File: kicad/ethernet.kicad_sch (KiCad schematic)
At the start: 6 parts, among them J1 RJ45_Abracon_ARJP11A-MASA-B-A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, U1 TM4C1294NCPDTI3

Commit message: board layout
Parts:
- removed U1: TM4C1294NCPDTI3, QFP40P1600X1600X120-128N, symbol TM4C1294NCPDTI3:TM4C1294NCPDTI3
- added C1, C10, C11, C12, C2, C3, C4, C5, C6, C7, C8, C9: 100n, Capacitor_SMD:C_0805_2012Metric, symbol Device:C_Small
- added C13: 4.7n, Capacitor_SMD:C_0805_2012Metric, symbol Device:C_Small
- added C14: 10n, Capacitor_SMD:C_0805_2012Metric, symbol Device:C_Small
- added J2: Conn_Coaxial, Connector_Coaxial:SMA_Molex_73251-2120_EdgeMount_Horizontal, symbol Connector:Conn_Coaxial
- added L1: 27n, Inductor_SMD:L_0805_2012Metric, symbol Device:L_Small
- added R10: 10, Resistor_SMD:R_0805_2012Metric, symbol Device:R_Small_US
- added R5, R6, R7: 10k, Resistor_SMD:R_0805_2012Metric, symbol Device:R_Small_US
- added R8: 1M, Resistor_SMD:R_0805_2012Metric, symbol Device:R_Small_US
- added R9: 4.87k, Resistor_SMD:R_0805_2012Metric, symbol Device:R_Small_US
- added U1: MSP432E401Y, Package_QFP:LQFP-128_14x14mm_P0.4mm, symbol MCU_Texas:MSP432E401Y
- added U2: MAX-8Q, RF_GPS:ublox_MAX, symbol RF_GPS:MAX-8Q
- added X1: TXEAADSANF-25.000000, Oscillator:Oscillator_SMD_SeikoEpson_SG8002CE-4Pin_3.2x2.5mm, symbol Oscillator:TXC-7C
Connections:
- net +3V3: now also C10.1, C11.1, C12.1, C4.1, C5.1, C6.1, C7.1, C8.1, C9.1, U1.101 (VDD), U1.113 (VDD), U1.122 (VDD), U1.16 (VDD), U1.26 (VDD), U1.28 (VDD), U1.39 (VDD), U1.47 (VDD), U1.51 (VDD), U1.52 (VDD), U1.69 (VDD), U1.7 (VDD), U1.79 (VDD), U1.90 (VDD), U2.6 (V_BCKP), U2.7 (VCC_IO), U2.8 (VCC), X1.4 (Vdd)
- net GND: now also C1.2, C10.2, C11.2, C12.2, C13.2, C14.2, C2.2, C3.2, C4.2, C5.2, C6.2, C7.2, C8.2, C9.2, J2.2 (Ext), R8.1, R9.1, U1.10 (GNDA), U1.114 (GND), U1.17 (GND), U1.48 (GND), U1.55 (GND), U1.58 (GND), U1.80 (GND), U2.1 (GND), U2.10 (GND), U2.12 (GND), X1.2 (GND)
- net at J1.1 (TD+), R4.2: now also U1.57 (EN0TXOP)
- net at J1.15 (SHIELD): now also C13.1, R8.2
- net at J1.2 (TD-), R3.1: now also U1.56 (EN0TXON)
- net at J1.3 (RD+), R2.2: now also U1.54 (EN0RXIP)
- net at J1.6 (RD-), R1.1: now also U1.53 (EN0RXIN)
- new net: J2.1 (In), L1.2, U2.11 (RF_IN)
- new net: R10.1, U2.14 (VCC_RF)
- new net: C14.1, L1.1, R10.2
- new net: C1.1, R5.2, R6.1
- new net: C2.1, R6.2, R7.1
- new net: C3.1, R7.2, X1.1 (EN)
- new net: U1.88 (OSC0), X1.3 (OUT)
- new net: R9.2, U1.59 (RBIAS)
- new net: R5.1, U1.93 (PL7)
- new net gPPS: U1.71 (PM7), U2.4 (TIMEPULSE)
- new net gRX: U1.96 (PB1), U2.3 (RXD)
- new net gTX: U1.95 (PB0), U2.2 (TXD)
- new net uPPS: U1.49 (PG0), U1.72 (PM6)

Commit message: board layout
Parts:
- added C15, C16: 100n, Capacitor_SMD:C_0805_2012Metric, symbol Device:C_Small
- added C17: 2.7u, Capacitor_SMD:C_0805_2012Metric, symbol Device:C_Small
- added J3: MSP-FET, Connector_PinHeader_2.54mm:PinHeader_2x07_P2.54mm_Vertical, symbol Connector_Generic:Conn_02x07_Odd_Even
- added R11, R12: 10k, Resistor_SMD:R_0805_2012Metric, symbol Device:R_Small_US
- added R13, R14: 330, Resistor_SMD:R_0805_2012Metric, symbol Device:R_Small_US
- added SW1, SW2: KSC701, Button_Switch_SMD:SW_Push_1P1T_NO_CK_KSC7xxJ, symbol Switch:SW_Push
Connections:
- net +3V3: now also U1.102 (PQ4), U1.103 (PP2), U1.104 (PP3), U1.105 (PP4), U1.106 (PP5), U1.107 (PN0), U1.108 (PN1), U1.109 (PN2), U1.110 (PN3), U1.111 (PN4), U1.112 (PN5), U1.43 (PF1), U1.44 (PF2), U1.45 (PF3), U1.50 (PG1), U1.60 (PK7), U1.61 (PK6), U1.62 (PK5), U1.63 (PK4), U1.68 (VBAT), U1.75 (PM3), U1.76 (PM2), U1.77 (PM1), U1.78 (PM0), U1.8 (VDDA), U1.81 (PL0), U1.82 (PL1), U1.83 (PL2), U1.84 (PL3), U1.85 (PL4), U1.86 (PL5), U1.9 (VREFA+), U1.91 (PB2), U1.92 (PB3), U1.94 (PL6), J3.4 (Pin_4), R11.2, R12.2
- net GND: now also J1.12 (LLED-), J1.14 (RLED-), C15.2, C16.2, C17.2, J3.9 (Pin_9), SW1.1, SW2.1
- net at J1.11 (LLED+): now also R13.2
- net at J1.13 (RLED+): now also R14.2
- net at U2.5 (EXTINT): now also U1.73 (PM5)
- net at U2.9 (~{RESET}): now also U1.74 (PM4)
- net at U1.100 (PC0/TCK/SWCLK): now also J3.7 (Pin_7)
- net at U1.115 (VDDC): now also U1.87 (VDDC), C15.1, C16.1, C17.1
- net ETH_LED0: now reaches U1.42 (PF0)
- net ETH_LED0: now also R13.1
- net ETH_LED1: now reaches U1.46 (PF4)
- net ETH_LED1: now also R14.1
- net ~{WAKE}: now reaches U1.64 (~{WAKE})
- net ~{WAKE}: now also R12.1, SW2.2
- net ~{RST}: now reaches U1.70 (~{RST})
- net ~{RST}: now also J3.11 (Pin_11), R11.1, SW1.2
- net at U1.97 (PC3/TDO/SWO): now also J3.1 (Pin_1)
- net at U1.98 (PC2/TDI): now also J3.3 (Pin_3)
- net at U1.99 (PC1/TMS/SWDIO): now also J3.5 (Pin_5)
- no-connect marks 0 -> 11

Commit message: board layout
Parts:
- added TR1: Wuerth_750315371, Transformer_SMD:Transformer_Wuerth_750315371, symbol Transformer:Wuerth_750315371
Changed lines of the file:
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@@
     (pin "2")
+  )
+  (symbol (lib_id "Transformer:Wuerth_750315371") (at 304.8 146.05 0) (unit 1)
+    (in_bom yes) (on_board yes) (fields_autoplaced)
+    (property "Reference" "TR1" (id 0) (at 304.8 139.9245 0))
+    (property "Value" "Wuerth_750315371" (id 1) (at 304.8 142.4614 0))
+    (property "Footprint" "Transformer_SMD:Transformer_Wuerth_750315371" (id 2) (at 304.8 153.035 0)
+      (effects (font (size 1.27 1.27)) hide)
+    )
+    (property "Datasheet" "https://www.we-online.com/catalog/datasheet/750315371.pdf" (id 3) (at 304.8 146.05 0)
+      (effects (font (size 1.27 1.27)) hide)
+    )
+    (pin "1")
+    (pin "2")
+    (pin "3")
+    (pin "4")
+    (pin "5")
+    (pin "6")
   )
   (symbol (lib_id "power:+3.3V") (at 76.2 172.72 90) (mirror x) (unit 1)
@@
       (reference "SW2") (unit 1) (value "KSC701") (footprint "Button_Switch_SMD:SW_Push_1P1T_NO_CK_KSC7xxJ")
     )
+    (path "/5410253c-a8cd-4a52-8c5d-a9cfceac5378"
+      (reference "TR1") (unit 1) (value "Wuerth_750315371") (footprint "Transformer_SMD:Transformer_Wuerth_750315371")
+    )
     (path "/62a86672-b56e-46bd-bc25-5c0442dd543c"

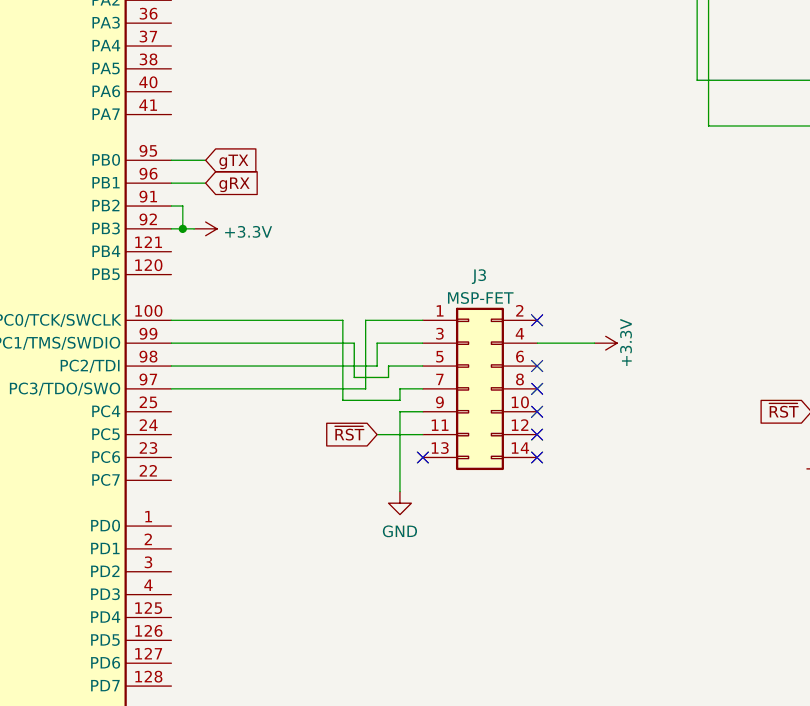
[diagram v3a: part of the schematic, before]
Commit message: begin PTP implementation
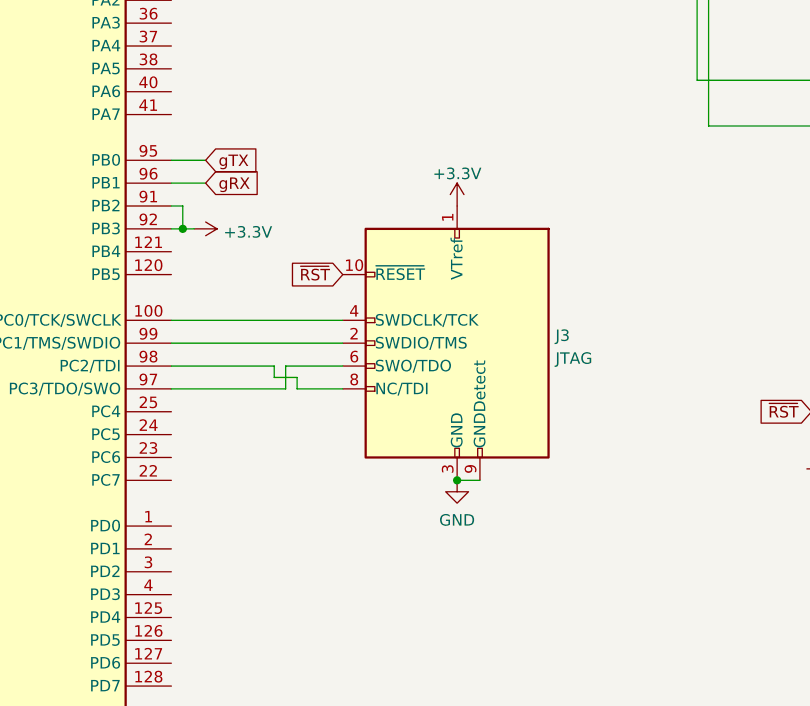
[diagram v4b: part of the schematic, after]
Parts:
- removed J3: MSP-FET, Connector_PinHeader_2.54mm:PinHeader_2x07_P2.54mm_Vertical, symbol Connector_Generic:Conn_02x07_Odd_Even
- added J3: JTAG, Connector_PinHeader_2.54mm:PinHeader_2x05_P2.54mm_Vertical, symbol Connector:Conn_ARM_JTAG_SWD_10
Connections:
- net +3V3: now also J3.1 (VTref)
- net GND: now also J3.3 (GND), J3.5 (GND), J3.9 (GNDDetect)
- net ~{RST}: now also J3.10 (~{RESET})
- net at U1.100 (PC0/TCK/SWCLK): now also J3.4 (SWDCLK/TCK)
- net at U1.97 (PC3/TDO/SWO): now also J3.6 (SWO/TDO)
- net at U1.98 (PC2/TDI): now also J3.8 (NC/TDI)
- net at U1.99 (PC1/TMS/SWDIO): now also J3.2 (SWDIO/TMS)
- no-connect marks 11 -> 4

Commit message: updating schematic
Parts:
- removed C3: 100n, Capacitor_SMD:C_0805_2012Metric, symbol Device:C_Small
- removed R6, R7: 10k, Resistor_SMD:R_0805_2012Metric, symbol Device:R_Small_US
- removed X1: TXEAADSANF-25.000000, Oscillator:Oscillator_SMD_SeikoEpson_SG8002CE-4Pin_3.2x2.5mm, symbol Oscillator:TXC-7C
- added BT1, BT2, BT3, BT4: NiMH, Battery:BatteryHolder_Keystone_2466_1xAAA, symbol Device:Battery_Cell
- added R15, R16, R17, R18: 110k, Resistor_SMD:R_0805_2012Metric, symbol Device:R_Small_US
- added R19, R20, R21, R22: 330k, Resistor_SMD:R_0805_2012Metric, symbol Device:R_Small_US
- added Y1: NX3225GA-25.000M-STD-CRG-2, Crystal:Crystal_SMD_3225-4Pin_3.2x2.5mm, symbol Device:Crystal_GND2
- C1, C2: value 100n -> 12p
- R5: value 10k -> 2k
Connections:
- net +3V3: now also U1.93 (PL7)
- net GND: now also C2.1, BT1.2 (-), R15.2, R16.2, R17.2, R18.2; no longer C2.2
- net at C1.1: now also U1.88 (OSC0), Y1.1; no longer R5.2
- net at U1.12 (PE3): now also R18.1, R22.2
- net at U1.13 (PE2): now also R17.1, R21.2
- net at U1.14 (PE1): now also R16.1, R20.2
- net at U1.15 (PE0): now also R15.1, R19.2
- net at U1.89 (OSC1): now also R5.1
- net uPPS renamed ePPS
- new net: BT2.1 (+), BT3.2 (-), R21.1
- new net: BT1.1 (+), BT2.2 (-), R22.1
- new net: C2.2, R5.2, Y1.3
- new net: BT4.1 (+), R19.1
- new net: BT3.1 (+), BT4.2 (-), R20.1
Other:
- note added: "Voltage Monitors"

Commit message: updating schematic
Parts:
- removed BT4: NiMH, Battery:BatteryHolder_Keystone_2466_1xAAA, symbol Device:Battery_Cell
- removed R15: 110k, Resistor_SMD:R_0805_2012Metric, symbol Device:R_Small_US
- removed R19: 330k, Resistor_SMD:R_0805_2012Metric, symbol Device:R_Small_US
- removed Y1: NX3225GA-25.000M-STD-CRG-2, Crystal:Crystal_SMD_3225-4Pin_3.2x2.5mm, symbol Device:Crystal_GND2
- added Y1: NX3225GA-25.000M-STD-CRG-2, Crystal:Crystal_SMD_3225-4Pin_3.2x2.5mm, symbol Device:Crystal_GND24
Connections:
- net GND: now also Y1.2, Y1.4
- net ePPS: now also U1.41 (PA7); no longer U1.72 (PM6)
- net gPPS: now also U1.40 (PA6); no longer U1.71 (PM7)
- net gRX: now also U1.34 (PA1); no longer U1.96 (PB1)
- net gTX: now also U1.33 (PA0); no longer U1.95 (PB0)
- net at C1.1, U1.88 (OSC0): now also Y1.1
- net at C2.2, R5.2: now also Y1.3

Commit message: update schematic
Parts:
- added C18, C19, C20: 10n, Capacitor_SMD:C_0805_2012Metric, symbol Device:C_Small
- added C3: 100n, Capacitor_SMD:C_0805_2012Metric, symbol Device:C_Small
- added D1, D3, D5: LED, LED_THT:LED_D5.0mm_Horizontal_O3.81mm_Z3.0mm, symbol Device:LED
- added D2, D4, D6: LED, LED_THT:LED_D5.0mm_Horizontal_O1.27mm_Z3.0mm, symbol Device:LED
- added J4: USB_C_Receptacle_USB2.0, Connector_USB:USB_C_Receptacle_XKB_U262-16XN-4BVC11, symbol Connector:USB_C_Receptacle_USB2.0
- added J5, J6: Conn_Coaxial, Connector_Coaxial:SMA_Molex_73251-2120_EdgeMount_Horizontal, symbol Connector:Conn_Coaxial
- added R15, R7: 5.1k, Resistor_SMD:R_0805_2012Metric, symbol Device:R_Small_US
- added R19, R23, R24, R25, R26, R27: 330, Resistor_SMD:R_0805_2012Metric, symbol Device:R_Small_US
- added R6: 49.9, Resistor_SMD:R_0805_2012Metric, symbol Device:R_Small_US
- added U3: TPD4S014, Package_SON:Texas_S-PWSON-N10, symbol Power_Protection:TPD4S014
- added U4, U5: 74AUC2G34, Package_TO_SOT_SMD:SOT-23-6, symbol 74xGxx:74AUC2G34
- R20, R21, R22: value 330k -> 220k
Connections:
- net +3V3: now also U1.36 (PA3), U1.38 (PA5), U4.5 (VCC), U4.5 (VCC), U5.5 (VCC), U5.5 (VCC); no longer U1.93 (PL7), U1.94 (PL6)
- net GND: now also C18.1, C19.1, C20.1, C3.2, D1.1 (K), D2.1 (K), D3.1 (K), D4.1 (K), D5.1 (K), D6.1 (K), J4.A1 (GND), J4.A12 (GND), J4.B1 (GND), J4.B12 (GND), J5.2 (Ext), J6.2 (Ext), R15.2, R7.2, U3.11 (PAD), U3.5 (ID), U3.8 (GND), U4.2 (GND), U4.2 (GND), U5.2 (GND), U5.2 (GND)
- net gPPS: now also U4.1
- net at U2.5 (EXTINT): now also U1.31 (PH2); no longer U1.73 (PM5)
- net at U2.9 (~{RESET}): now also U1.32 (PH3); no longer U1.74 (PM4)
- net +BATT: now reaches BT3.1 (+), R20.1
- net at R16.1, R20.2, U1.14 (PE1): now also C18.2
- net at R18.1, R22.2, U1.12 (PE3): now also C20.2
- net uPPS: now reaches U1.127 (PD6)
- net uPPS: now also U1.37 (PA4), U4.3, U5.1
- net at R17.1, R21.2, U1.13 (PE2): now also C19.2
- net uFRQ: now reaches U1.35 (PA2)
- net uFRQ: now also U5.3
- new net: D3.2 (A), R24.1
- new net: J5.1 (In), U4.4
- new net: D6.2 (A), R27.1
- new net: D2.2 (A), R23.1
- new net: D5.2 (A), R26.1
- new net: J4.B5 (CC2), R15.1
- new net: R25.2, U5.6
- new net: J6.1 (In), U5.4
- new net: D4.2 (A), R25.1
- new net: U3.1 (VBUSOUT), U3.2 (VBUSOUT)
- new net: D1.2 (A), R19.1
- new net: J4.A5 (CC1), R7.1
- new net: J4.S1 (SHIELD), R6.2
- new net: R23.2, U4.6
- new net: C3.1, R6.1
- new net D+: J4.A6 (D+), J4.B6 (D+), U1.94 (PL6), U3.7 (D+)
- new net D-: J4.A7 (D-), J4.B7 (D-), U1.93 (PL7), U3.6 (D-)
- new net VBUS: J4.A4 (VBUS), J4.A9 (VBUS), J4.B4 (VBUS), J4.B9 (VBUS), U3.10 (VBUS), U3.9 (VBUS)
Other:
- moved on the sheet: TR1

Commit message: poe supply design
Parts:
- added C21, C22: 10u, Capacitor_SMD:C_0805_2012Metric, symbol Device:C_Small
- added C23, C24: 100n, Capacitor_SMD:C_0805_2012Metric, symbol Device:C_Small
- added D7, D8: MBR0520L, Diode_SMD:D_SOD-123, symbol Device:D_Schottky
- added L2: LSXBH8080YKL101M, symbol Device:L_Small
- added Q1: BSO220N03MD, Package_SO:SOIC-8_3.9x4.9mm_P1.27mm, symbol Device:Q_Dual_NMOS_S1G1S2G2D2D2D1D1
- added R28, R29: 10k, Resistor_SMD:R_0805_2012Metric, symbol Device:R_Small_US
- added U6: MAX40200AUK, Package_TO_SOT_SMD:SOT-23-5, symbol Analog_Switch:MAX40200AUK
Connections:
- net +3V3: now also R28.2
- net GND: now also TR1.5, C22.1, C23.1, U6.2 (GND)
- net at TR1.1: now also Q1.4 (G), Q1.7 (D), Q1.8 (D)
- net at TR1.2: now also C21.1, C24.1
- net at TR1.3: now also Q1.2 (G), Q1.5 (D), Q1.6 (D)
- net at TR1.4: now also D8.2 (A)
- net at TR1.6: now also D7.2 (A)
- net +5V: now reaches U3.1 (VBUSOUT), U3.2 (VBUSOUT)
- net +5V: now also U6.5 (OUT)
- net at U3.3 (~{EN}): now also R29.1
- net VUSB: now reaches U3.4 (~{ACK})
- net VUSB: now also R28.1
- new net: C21.2, C24.2, L2.1
- new net: L2.2, Q1.1 (S), Q1.3 (S)
- new net +5VP: C22.2, C23.2, D7.1 (K), D8.1 (K), R29.2, U6.1 (VDD), U6.3 (EN)
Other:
- moved on the sheet: TR1
